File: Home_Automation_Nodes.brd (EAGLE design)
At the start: 120.1 x 69.5 mm, 16 parts

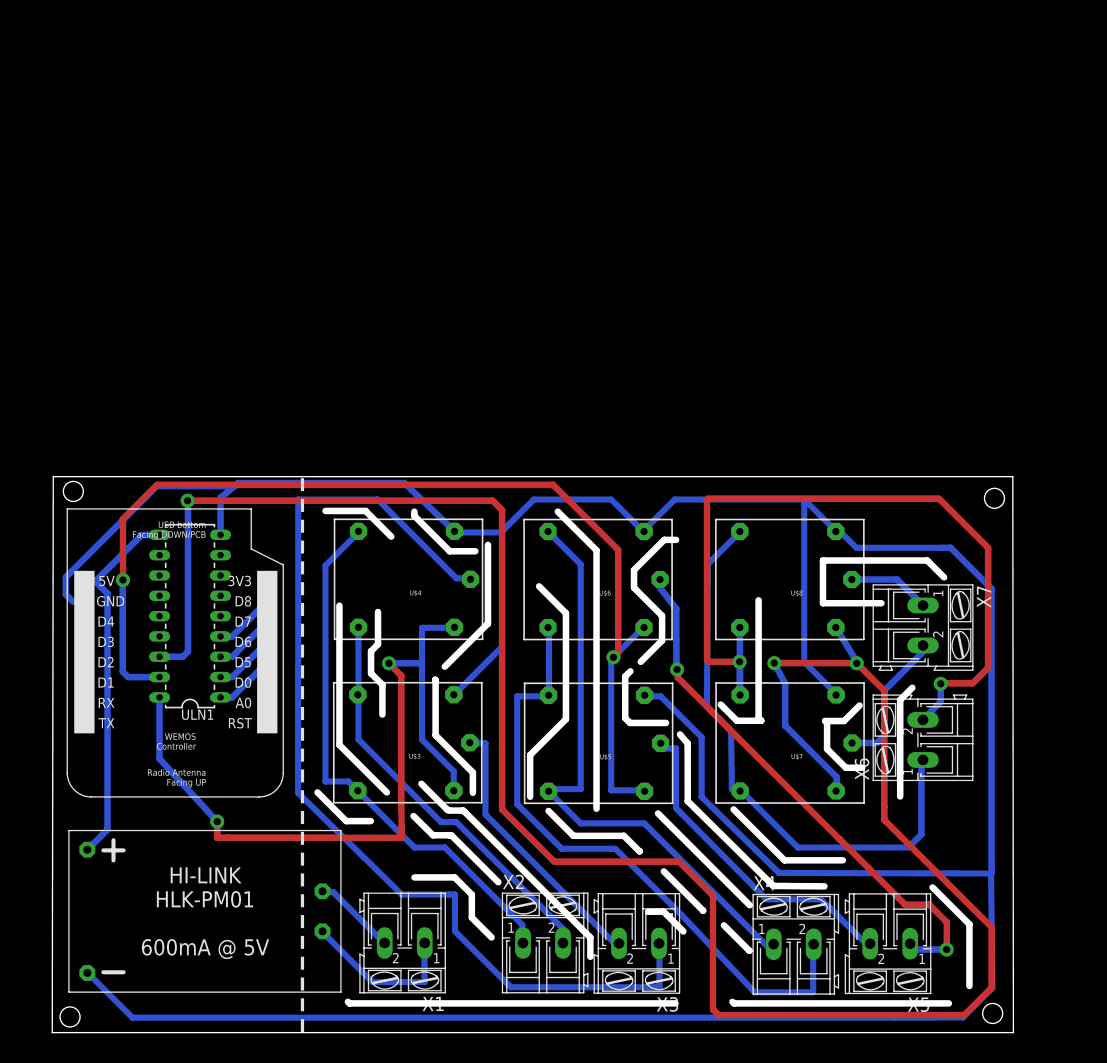
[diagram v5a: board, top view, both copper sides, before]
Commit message: 100 mils spacing Top Bottom routing.No Vias
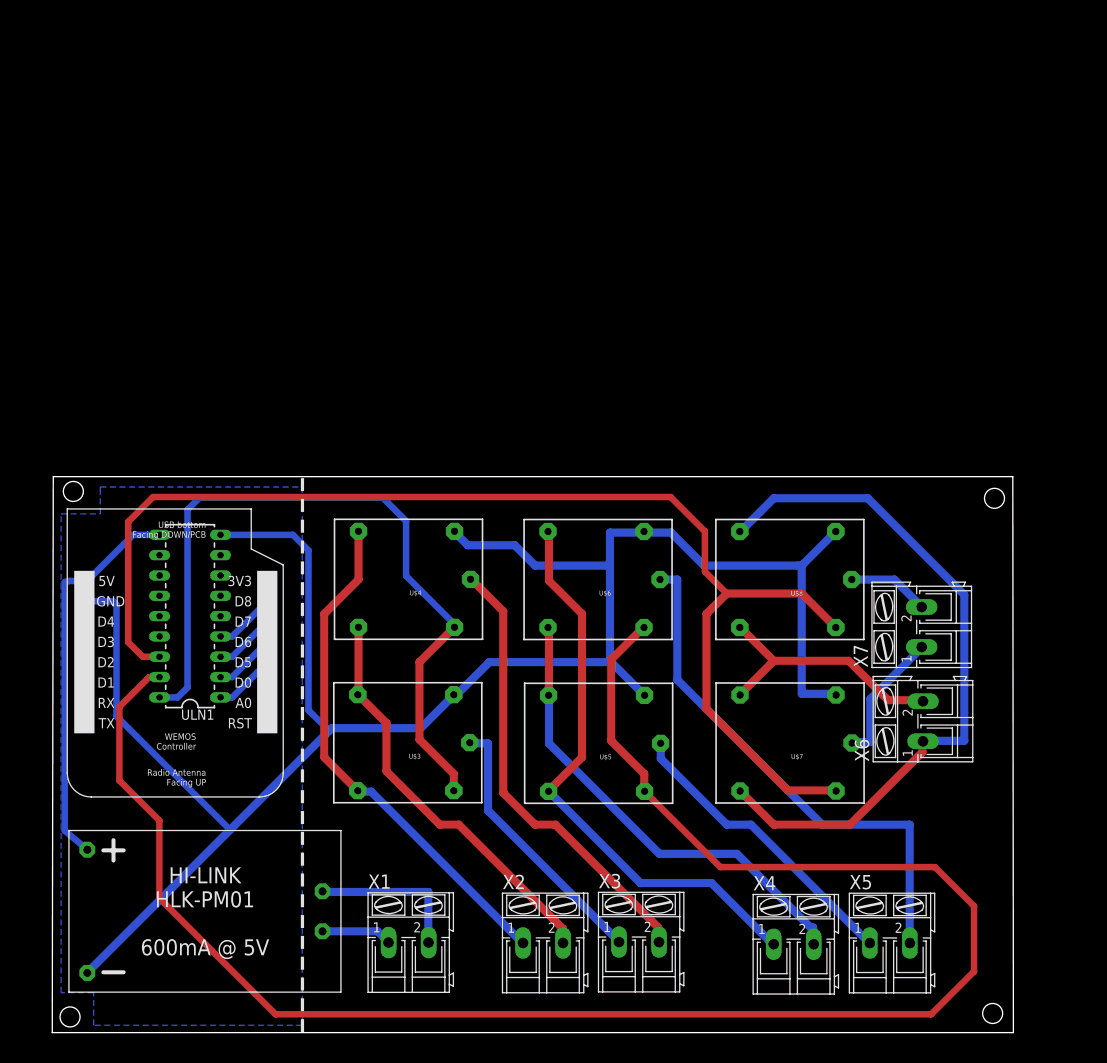
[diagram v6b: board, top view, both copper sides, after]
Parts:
- moved X6 2.33 mm to (108.8, 39.0)
- moved X1 0.51 mm to (44.5, 11.3), turned to 0 degrees
- moved X7 0.23 mm to (108.7, 50.8), turned to 90 degrees
- moved X3 0.17 mm to (73.3, 11.4), turned to 0 degrees
- moved X5 0.08 mm to (104.7, 11.2), turned to 0 degrees
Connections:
- removed net N$17: U$5.SWCOMMON, X5.2
- removed net N$23: U$7.SWCOMMON, X7.2
- removed net N$9: U$3.SWCOMMON, X3.2
- new net N$3: U$3.SWCOMMON, X3.1
- new net N$4: U$5.SWCOMMON, X5.1
- new net N$7: U$7.SWCOMMON, X7.1
- net N$10: now also X3.2; no longer X3.1
- net N$18: now also X5.2; no longer X5.1
- net N$24: now also X7.2; no longer X7.1
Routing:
- net GND: track 417.1 -> 250.7 mm
- net RELAY3: track 263.6 -> 155.1 mm, vias 3 -> 0
- net RELAY2: track 131.8 -> 221.8 mm, vias 2 -> 0
- net N$10: track 125.7 -> 56.7 mm
- net N$20: track 101.7 -> 32.7 mm, vias 2 -> 0
- net N$17: track 42.1 -> 0.00 mm
- net N$4: track 0.00 -> 37.6 mm
- net N$9: track 35.0 -> 0.00 mm
- net N$3: track 0.00 -> 33.9 mm
- net N$12: track 78.9 -> 59.3 mm
- net N$23: track 17.7 -> 0.00 mm
- net N$7: track 0.00 -> 16.9 mm
- net N$19: track 72.0 -> 87.9 mm
- net N$2: track 20.5 -> 8.85 mm
- net N$1: track 10.5 -> 19.6 mm
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- added copper zone on layer 16, net N$8
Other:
- outline, holes or cut-outs redrawn
- board text added: "AC Main IN"
- board text added: "Incoming Line"
- board text added: "Outcoming Line"

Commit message: Changes: 1. SCH: Added decoupling capacitor. Breakout for A0 and 4 digital pins 2. BRD: 100 mils spacing, 80 mils track width. Legends added
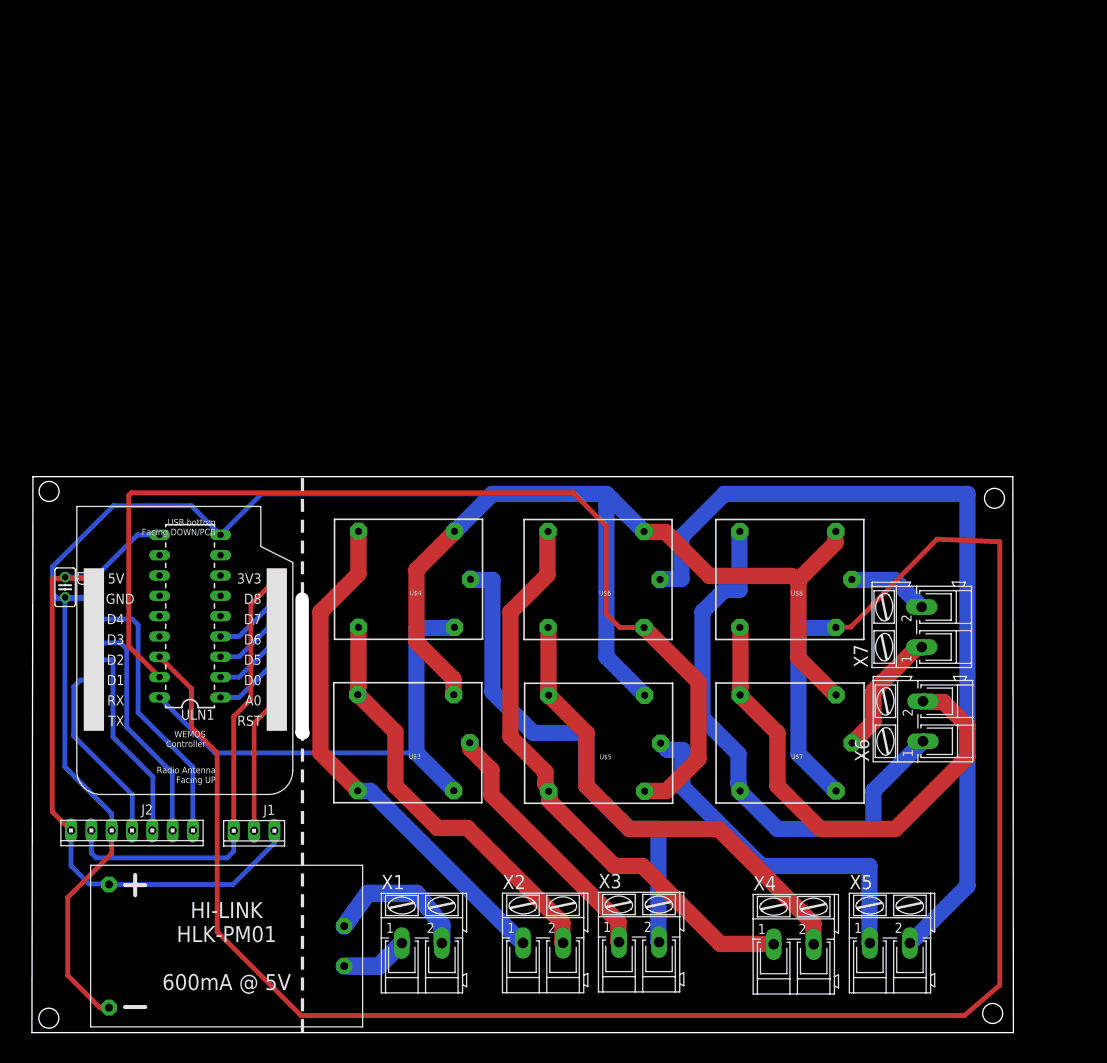
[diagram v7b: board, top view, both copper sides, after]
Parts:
- added C1: 0.1uF, rcl:C025-025X050
- added J1: (no value), con-amp:10X03MTA
- added J2: (no value), con-amp:10X07MTA
- moved U$2 5.12 mm to (21.8, 10.9)
- moved X1 1.66 mm to (46.2, 11.2)
- moved U$1 1.23 mm to (28.0, 56.8)
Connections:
- new net A0: J1.2, U$1.A0
- new net D1: J2.4, U$1.D1
- new net D2: J2.5, U$1.D2
- new net D3: J2.6, U$1.D3
- new net D4: J2.7, U$1.D4
- new net N$16: U$1.RX
- new net N$17: U$1.TX
- net 3.3V: now also J1.1, J2.2
- net 5V: now also C1.1, J1.3, J2.1
- net GND: now also C1.2, J2.3
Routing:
- net RELAY3: track 155.1 -> 248.5 mm
- net RELAY2: track 221.8 -> 129.9 mm
- net 3.3V: track 0.00 -> 57.5 mm
- net N$18: track 66.1 -> 105.1 mm
- net 5V: track 49.0 -> 86.3 mm
- net D4: track 0.00 -> 34.4 mm
- net RELAY1: track 96.2 -> 62.1 mm
- net D3: track 0.00 -> 29.7 mm
- net N$20: track 32.7 -> 62.2 mm
- net D2: track 0.00 -> 25.8 mm
- net D1: track 0.00 -> 23.9 mm
- net N$19: track 87.9 -> 69.6 mm
- net A0: track 0.00 -> 17.5 mm
- net GND: track 250.7 -> 258.0 mm
- net N$4: track 37.6 -> 44.8 mm
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- removed copper zone on layer 16, net N$8
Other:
- board size 120.1 x 69.5 mm -> 122.7 x 69.5 mm

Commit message: Final version. Sent to Mervin for verification
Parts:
- moved U$3 1.05 mm to (45.8, 36.4)
- moved U$4 1.05 mm to (45.9, 56.8)
- moved U$7 1.05 mm to (93.6, 36.3)
- moved U$8 1.05 mm to (93.6, 56.8)
- moved ULN1 1.05 mm to (18.2, 52.3)
- moved X7 1.05 mm to (109.7, 51.0)
- moved U$2 1.05 mm to (22.8, 11.1)
- moved X1 1.05 mm to (47.2, 11.4)
- moved X2 1.05 mm to (62.4, 11.4)
- moved X3 1.05 mm to (74.4, 11.6)
- moved X4 1.05 mm to (93.7, 11.3)
- moved X5 1.05 mm to (105.7, 11.4)
- moved U$5 1.05 mm to (69.7, 36.3)
- moved U$6 1.05 mm to (69.6, 56.8)
- moved X6 1.05 mm to (109.8, 39.2)
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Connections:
- net 5V: no longer J1.3
- net GND: now also J1.3
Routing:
- net GND: track 258.0 -> 288.8 mm
- net 5V: track 86.3 -> 62.1 mm
- net N$18: track 105.1 -> 101.7 mm
- added copper zone on layer 16, net GND
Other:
- board size 122.7 x 69.5 mm -> 121 x 70 mm
- board text added: "3.3V"
- board text added: "4 Way Switching Home Automation Node v0.6"
- board text added: "5V"
- board text added: "A0"
- board text added: "D1"
- board text added: "D2"
- board text added: "D3"
- board text added: "D4"
- board text added: "GND"
- board text added: "Outgoing Line"
- board text removed: "Outcoming Line"
